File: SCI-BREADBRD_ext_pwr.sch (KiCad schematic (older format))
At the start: 8 parts, among them P3 CONN_3, Q1 SI4564DY-T1-GE3

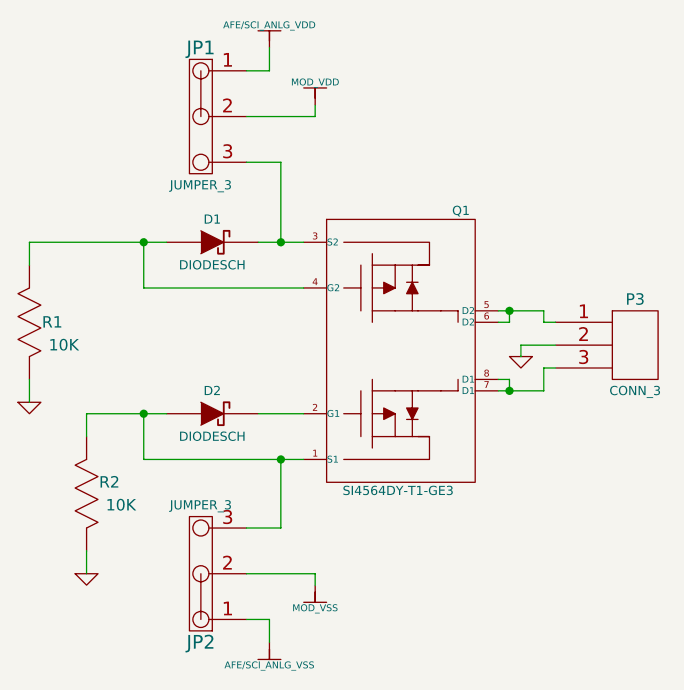
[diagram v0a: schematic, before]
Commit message: Completed ERC. Added some power flags and fixed mis-connected pins.
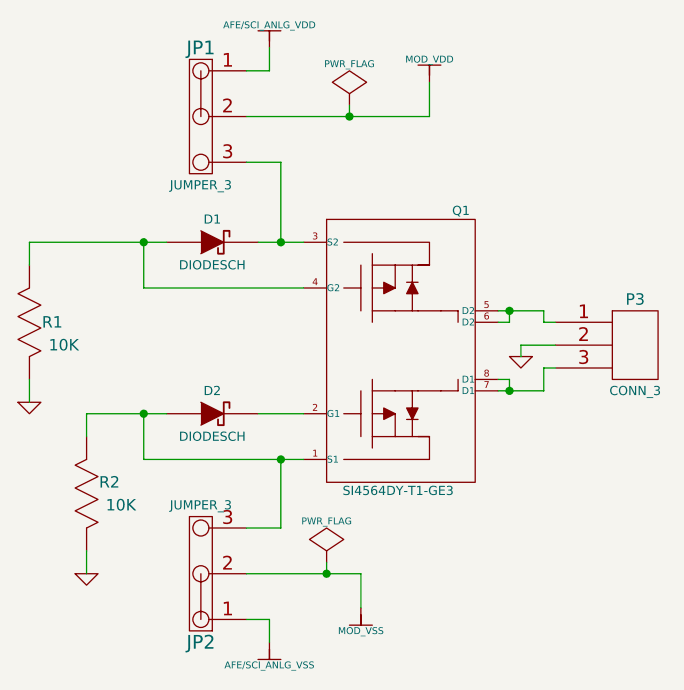
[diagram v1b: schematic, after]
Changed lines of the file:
@@
-EESchema Schematic File Version 2  date Fri 27 Apr 2012 09:11:54 AM EDT
+EESchema Schematic File Version 2  date Fri 27 Apr 2012 11:11:24 AM EDT
 LIBS:custom_transistors
 LIBS:TI_custom
@@
 L MOD_VSS #PWR012
 U 1 1 4F9A637A
-P 5950 4600
-F 0 "#PWR012" H 5950 4500 30  0001 C CNN
-F 1 "MOD_VSS" H 5950 4500 30  0000 C CNN
-	1    5950 4600
+P 6150 4700
+F 0 "#PWR012" H 6150 4600 30  0001 C CNN
+F 1 "MOD_VSS" H 6150 4600 30  0000 C CNN
+	1    6150 4700
 	1    0    0    -1
 $EndComp
@@
 L MOD_VDD #PWR013
 U 1 1 4F9A6380
-P 5950 2500
-F 0 "#PWR013" H 5950 2600 30  0001 C CNN
-F 1 "MOD_VDD" H 5950 2600 30  0000 C CNN
-	1    5950 2500
+P 6450 2400
+F 0 "#PWR013" H 6450 2500 30  0001 C CNN
+F 1 "MOD_VDD" H 6450 2500 30  0000 C CNN
+	1    6450 2400
+	1    0    0    -1
+$EndComp
+$Comp
+L PWR_FLAG #FLG014
+U 1 1 4F9AE522
+P 6100 2500
+F 0 "#FLG014" H 6100 2595 30  0001 C CNN
+F 1 "PWR_FLAG" H 6100 2680 30  0000 C CNN
+	1    6100 2500
+	1    0    0    -1
+$EndComp
+$Comp
+L PWR_FLAG #FLG015
+U 1 1 4F9AE5B3
+P 6000 4500
+F 0 "#FLG015" H 6000 4595 30  0001 C CNN
+F 1 "PWR_FLAG" H 6000 4680 30  0000 C CNN
+	1    6000 4500
 	1    0    0    -1
 $EndComp
@@
 	6850 3550 7000 3550
 Wire Wire Line
-	5700 3100 5900 3100
-Wire Wire Line
 	5800 3100 5800 2750
 Wire Wire Line
@@
 	5700 3850 5900 3850
 Wire Wire Line
-	5200 4050 5900 4050
-Wire Wire Line
 	5200 4050 5200 3850
 Connection ~ 5200 3850
@@
 	4950 3850 5300 3850
 Wire Wire Line
-	5950 4600 5950 4550
-Wire Wire Line
-	5950 4550 5650 4550
-Wire Wire Line
-	5650 2550 5950 2550
-Wire Wire Line
-	5950 2550 5950 2500
+	6150 4700 6150 4550
+Wire Wire Line
+	6150 4550 5650 4550
+Wire Wire Line
+	5650 2550 6450 2550
+Wire Wire Line
+	6450 2550 6450 2400
+Wire Wire Line
+	5700 3100 5900 3100
+Wire Wire Line
+	5200 4050 5900 4050
+Wire Wire Line
+	6100 2500 6100 2550
+Connection ~ 6100 2550
+Wire Wire Line
+	6000 4500 6000 4550
+Connection ~ 6000 4550
 $EndSCHEMATC

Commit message: Fixed more component properties to make the BOM look nice
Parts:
- R1, R2: Description RES Thick Film 10K OHM 1/10W ±5% 0402 -> RES Thick Film 10K OHM 1/10W 5% 0402
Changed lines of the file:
@@
-EESchema Schematic File Version 2  date Fri 27 Apr 2012 11:11:24 AM EDT
+EESchema Schematic File Version 2  date Fri 27 Apr 2012 12:42:01 PM EDT
 LIBS:custom_transistors
 LIBS:TI_custom
@@
 F 4 "Panasonic - ECG" H 4950 4200 60  0001 C CNN "Manufacturer"
 F 5 "ERJ-2GEJ103X" H 4950 4200 60  0001 C CNN "Part Number"
-F 6 "RES Thick Film 10K OHM 1/10W ±5% 0402" H 4950 4200 60  0001 C CNN "Description"
+F 6 "RES Thick Film 10K OHM 1/10W 5% 0402" H 4950 4200 60  0001 C CNN "Description"
 	1    4950 4200
 	0    -1   -1   0
@@
 F 4 "Panasonic - ECG" H 4700 3450 60  0001 C CNN "Manufacturer"
 F 5 "ERJ-2GEJ103X" H 4700 3450 60  0001 C CNN "Part Number"
-F 6 "RES Thick Film 10K OHM 1/10W ±5% 0402" H 4700 3450 60  0001 C CNN "Description"
+F 6 "RES Thick Film 10K OHM 1/10W 5% 0402" H 4700 3450 60  0001 C CNN "Description"
 	1    4700 3450
 	0    -1   -1   0

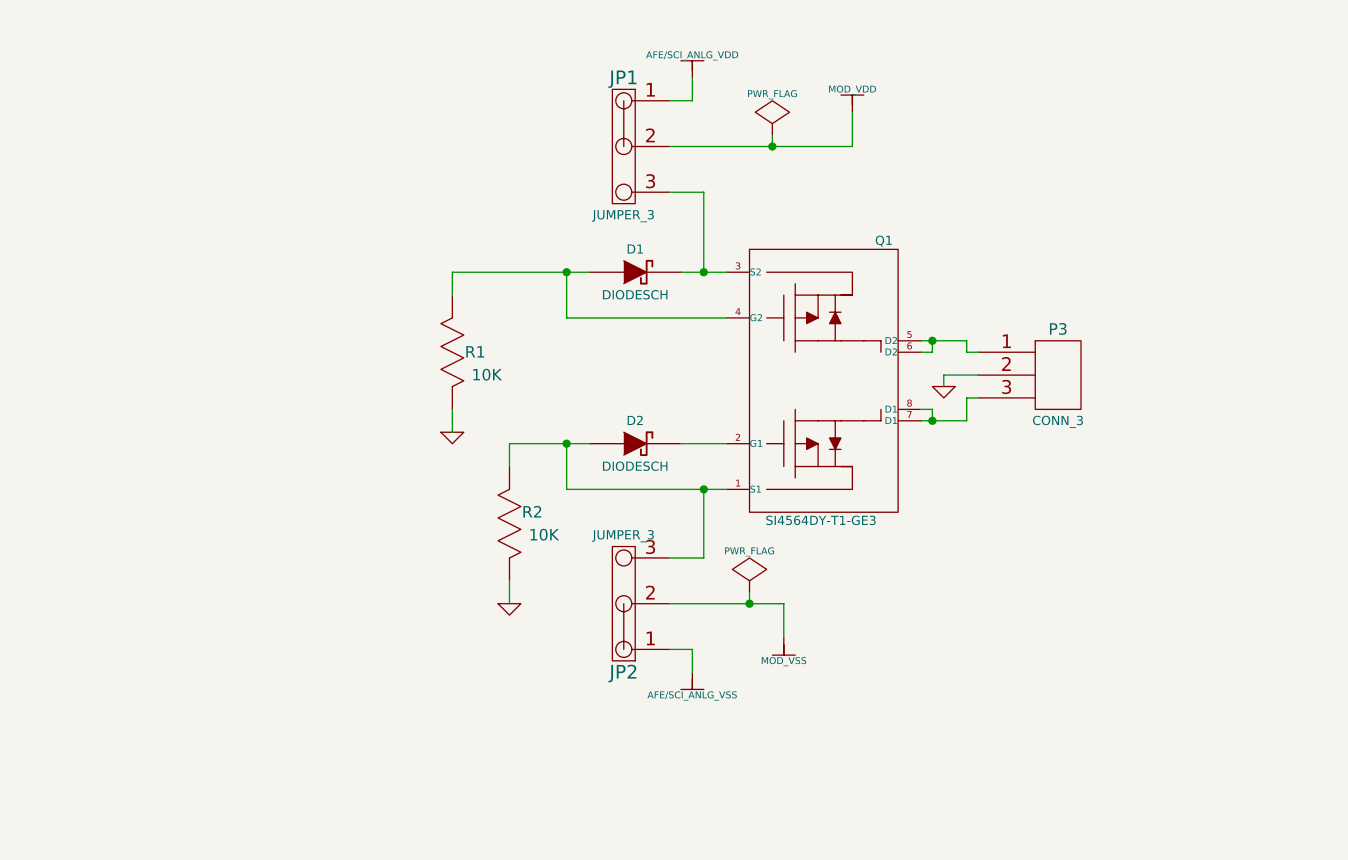
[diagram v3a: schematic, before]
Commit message: Enlarged the text on all of the power rails to make them easier to see when plotted
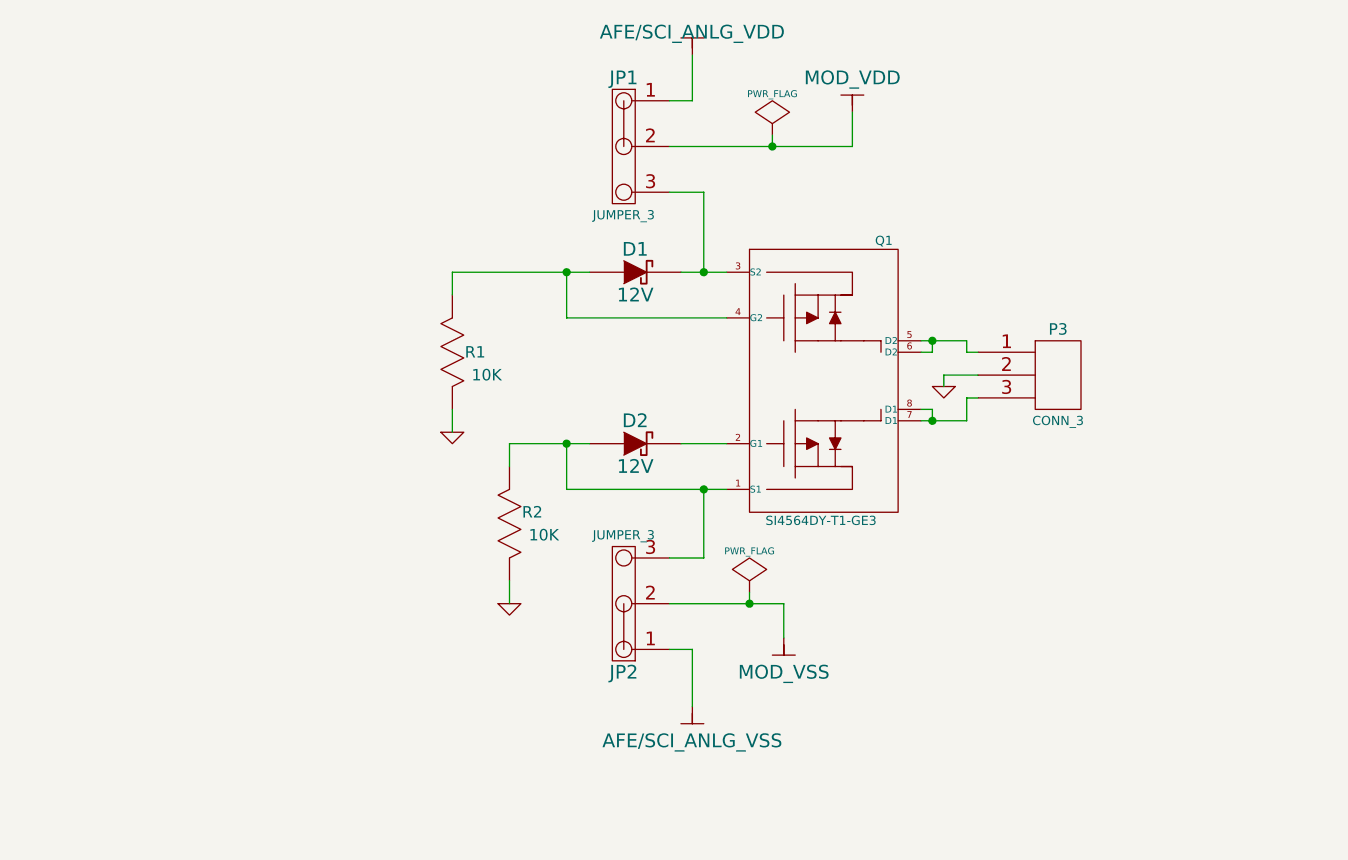
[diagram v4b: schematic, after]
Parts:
- D1, D2: value DIODESCH -> 12V
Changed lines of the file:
@@
-EESchema Schematic File Version 2  date Fri 27 Apr 2012 01:15:52 PM EDT
+EESchema Schematic File Version 2  date Fri 27 Apr 2012 02:46:40 PM EDT
 LIBS:custom_transistors
 LIBS:TI_custom
@@
 U 1 1 4F9A6353
 P 5500 3100
-F 0 "D1" H 5500 3200 40  0000 C CNN
-F 1 "DIODESCH" H 5500 3000 40  0000 C CNN
+F 0 "D1" H 5500 3200 60  0000 C CNN
+F 1 "12V" H 5500 3000 60  0000 C CNN
 F 2 "SOT_23_ON" H 5500 3100 60  0001 C CNN
 F 4 "ON Semiconductor" H 5500 3100 60  0001 C CNN "Manufacturer"
@@
 U 1 1 4F9A635C
 P 5500 3850
-F 0 "D2" H 5500 3950 40  0000 C CNN
-F 1 "DIODESCH" H 5500 3750 40  0000 C CNN
+F 0 "D2" H 5500 3950 60  0000 C CNN
+F 1 "12V" H 5500 3750 60  0000 C CNN
 F 2 "SOT_23_ON" H 5500 3850 60  0001 C CNN
 F 4 "ON Semiconductor" H 5500 3850 60  0001 C CNN "Manufacturer"
@@
 $EndComp
 $Comp
-L AFE/SCI_ANLG_VDD #PWR9
-U 1 1 4F9A636E
-P 5750 2250
-F 0 "#PWR9" H 5750 2350 30  0001 C CNN
-F 1 "AFE/SCI_ANLG_VDD" H 5750 2350 30  0000 C CNN
-	1    5750 2250
-	1    0    0    -1
-$EndComp
-$Comp
-L AFE/SCI_ANLG_VSS #PWR10
-U 1 1 4F9A6374
-P 5750 4850
-F 0 "#PWR10" H 5750 4750 30  0001 C CNN
-F 1 "AFE/SCI_ANLG_VSS" H 5750 4750 30  0000 C CNN
-	1    5750 4850
-	1    0    0    -1
-$EndComp
-$Comp
-L MOD_VSS #PWR11
-U 1 1 4F9A637A
-P 6150 4700
-F 0 "#PWR11" H 6150 4600 30  0001 C CNN
-F 1 "MOD_VSS" H 6150 4600 30  0000 C CNN
-	1    6150 4700
-	1    0    0    -1
-$EndComp
-$Comp
-L MOD_VDD #PWR12
-U 1 1 4F9A6380
-P 6450 2400
-F 0 "#PWR12" H 6450 2500 30  0001 C CNN
-F 1 "MOD_VDD" H 6450 2500 30  0000 C CNN
-	1    6450 2400
-	1    0    0    -1
-$EndComp
-$Comp
 L PWR_FLAG #FLG2
 U 1 1 4F9AE522
@@
 	1    0    0    -1
 $EndComp
-Wire Wire Line
-	6750 3400 6950 3400
+$Comp
+L MOD_VDD #PWR?
+U 1 1 4F9AEB3C
+P 6450 2400
+F 0 "#PWR?" H 6450 2500 30  0001 C CNN
+F 1 "MOD_VDD" H 6450 2550 60  0000 C CNN
+	1    6450 2400
+	1    0    0    -1
+$EndComp
+$Comp
+L MOD_VSS #PWR?
+U 1 1 4F9AEBAB
+P 6150 4700
+F 0 "#PWR?" H 6150 4600 30  0001 C CNN
+F 1 "MOD_VSS" H 6150 4550 60  0000 C CNN
+	1    6150 4700
+	1    0    0    -1
+$EndComp
+$Comp
+L AFE/SCI_ANLG_VDD #PWR?
+U 1 1 4F9AEBBA
+P 5750 2150
+F 0 "#PWR?" H 5750 2250 30  0001 C CNN
+F 1 "AFE/SCI_ANLG_VDD" H 5750 2250 60  0000 C CNN
+	1    5750 2150
+	1    0    0    -1
+$EndComp
+Wire Wire Line
+	6750 3400 6800 3400
+Wire Wire Line
+	6800 3400 6950 3400
 Wire Wire Line
 	6800 3400 6800 3450
@@
 	6800 3700 6800 3750
 Wire Wire Line
-	6750 3750 6950 3750
+	6750 3750 6800 3750
+Wire Wire Line
+	6800 3750 6950 3750
 Wire Wire Line
 	6950 3750 6950 3650
@@
 Connection ~ 5800 3100
 Wire Wire Line
-	4700 3100 5300 3100
+	4700 3100 5200 3100
+Wire Wire Line
+	5200 3100 5300 3100
 Wire Wire Line
 	4700 3800 4700 3700
@@
 Connection ~ 5800 4050
 Wire Wire Line
-	5650 2350 5750 2350
-Wire Wire Line
-	5750 2350 5750 2250
-Wire Wire Line
-	5750 4850 5750 4750
+	5750 2350 5650 2350
+Wire Wire Line
+	5750 2150 5750 2350
+Wire Wire Line
+	5750 5000 5750 4750
 Wire Wire Line
 	5750 4750 5650 4750
@@
 	4950 3950 4950 3850
 Wire Wire Line
-	4950 3850 5300 3850
+	4950 3850 5200 3850
+Wire Wire Line
+	5200 3850 5300 3850
 Wire Wire Line
 	6150 4700 6150 4550
 Wire Wire Line
-	6150 4550 5650 4550
-Wire Wire Line
-	5650 2550 6450 2550
+	6150 4550 6000 4550
+Wire Wire Line
+	6000 4550 5650 4550
+Wire Wire Line
+	5650 2550 6100 2550
+Wire Wire Line
+	6100 2550 6450 2550
 Wire Wire Line
 	6450 2550 6450 2400
 Wire Wire Line
-	5700 3100 5900 3100
-Wire Wire Line
-	5200 4050 5900 4050
+	5700 3100 5800 3100
+Wire Wire Line
+	5800 3100 5900 3100
+Wire Wire Line
+	5200 4050 5800 4050
+Wire Wire Line
+	5800 4050 5900 4050
 Wire Wire Line
 	6100 2500 6100 2550
@@
 	6000 4500 6000 4550
 Connection ~ 6000 4550
+$Comp
+L AFE/SCI_ANLG_VSS #PWR?
+U 1 1 4F9AEC2F
+P 5750 5000
+F 0 "#PWR?" H 5750 4900 30  0001 C CNN
+F 1 "AFE/SCI_ANLG_VSS" H 5750 4850 60  0000 C CNN
+	1    5750 5000
+	1    0    0    -1
+$EndComp
 $EndSCHEMATC

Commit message: Added breakout connector for external power. Removed useless jumpers to select between external/internal power
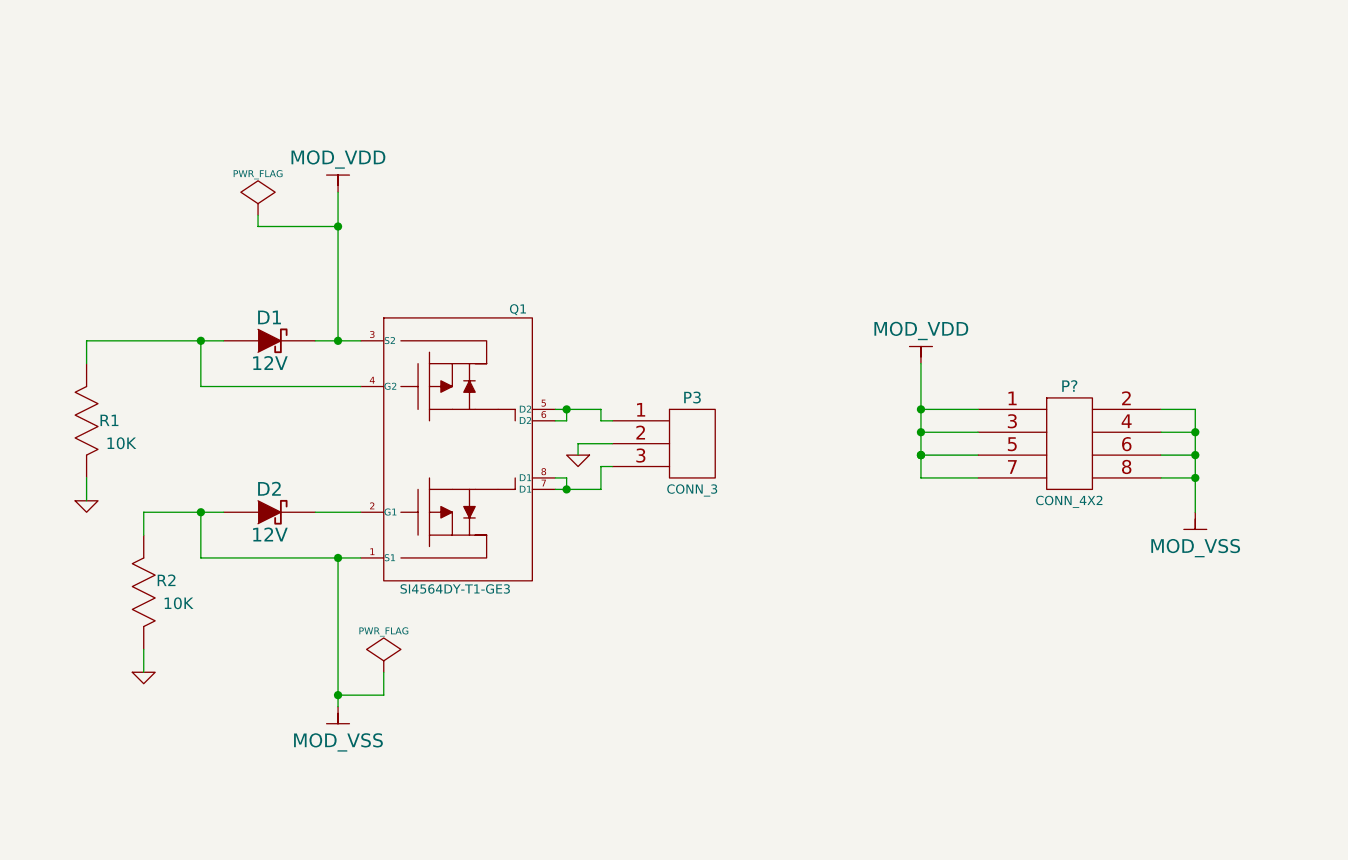
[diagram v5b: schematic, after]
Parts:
- removed JP1, JP2: JUMPER_3, PIN_ARRAY_3X1, symbol JUMPER_3
- added P?: CONN_4X2, pin_array_4x2, symbol CONN_4X2
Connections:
- net MOD_VDD: now also D1.2 (K), Q1.3 (S2), P?.1, P?.3, P?.5, P?.7
- net MOD_VSS: now also D2.1 (A), Q1.1 (S1), R2.2 (B), P?.2, P?.4, P?.6, P?.8
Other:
- moved on the sheet: D1, D2, P3, Q1, R1, R2
